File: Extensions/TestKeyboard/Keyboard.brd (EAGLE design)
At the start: 157.5 x 59.7 mm, 69 parts

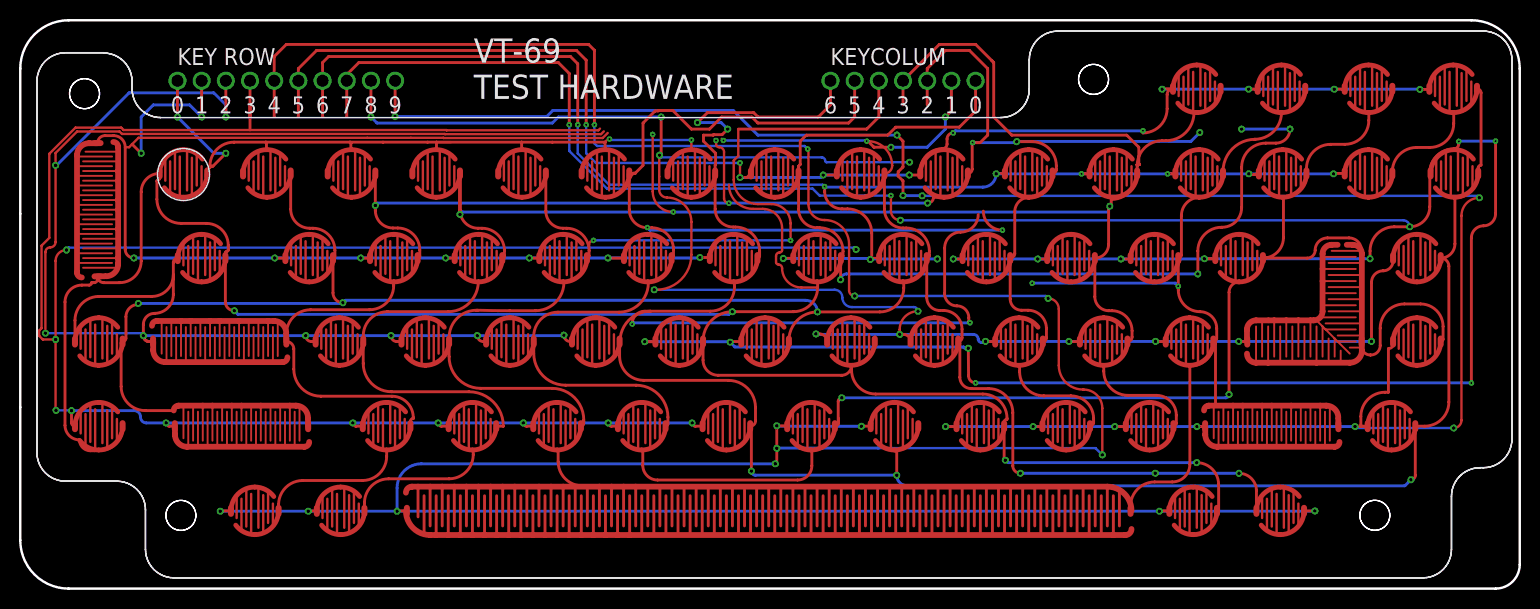
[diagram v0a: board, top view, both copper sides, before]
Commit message: changed MCU test board for FPC cable, other mods, moved test keyboard
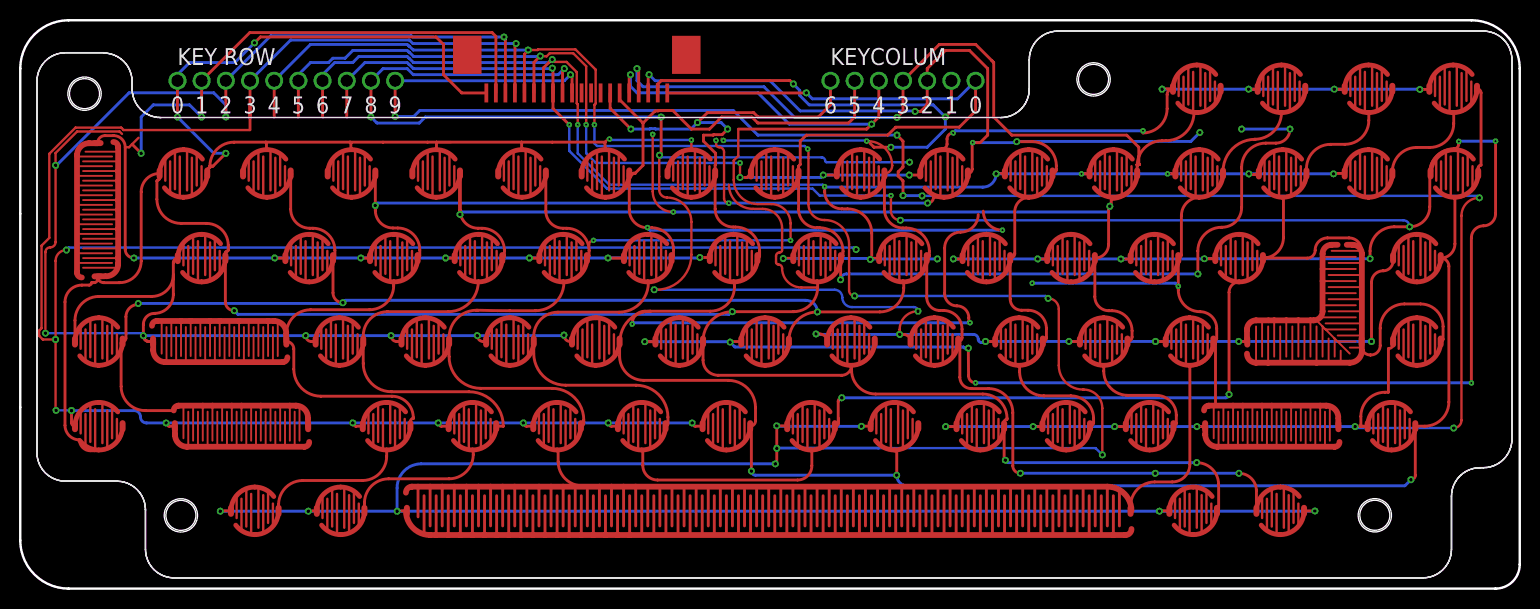
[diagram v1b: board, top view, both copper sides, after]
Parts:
- added U$1: FC1-20-L2-T-WT20PIN, FPC:FC1-20-L2-T-WT
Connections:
- new net KEYCOLUM0: U$1.20
- new net KEYCOLUM1: U$1.19
- new net KEYCOLUM2: U$1.18
- new net KEYCOLUM3: U$1.17
- new net KEYCOLUM4: U$1.16
- new net KEYCOLUM5: U$1.15
- new net KEYCOLUM6: U$1.14
- new net KEYROW0: U$1.1
- new net KEYROW1: U$1.2
- new net KEYROW2: U$1.3
- new net KEYROW3: U$1.4
- new net KEYROW4: U$1.5
- new net KEYROW5: U$1.6
- new net KEYROW6: U$1.7
- new net KEYROW7: U$1.8
- new net KEYROW8: U$1.9
- new net KEYROW9: U$1.10
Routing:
- net KEYROW0: track 100.3 -> 139.4 mm, vias 5 -> 6
- net KEYCOLUM3: track 239.7 -> 274.1 mm, vias 5 -> 7
- net KEYCOLUM0: track 331.6 -> 365.0 mm, vias 9 -> 10
- net KEYCOLUM1: track 241.2 -> 274.3 mm, vias 11 -> 12
- net KEYCOLUM2: track 232.4 -> 265.4 mm, vias 8 -> 10
- net KEYCOLUM4: track 265.3 -> 295.4 mm, vias 5 -> 7
- net KEYROW8: track 190.3 -> 214.3 mm, vias 14 -> 15
- net KEYROW9: track 221.1 -> 241.7 mm, vias 12 -> 13
- net KEYROW2: track 190.7 -> 177.1 mm, vias 9 -> 10
- net KEYCOLUM6: track 270.7 -> 282.7 mm, vias 8 -> 9
- net KEYROW1: track 149.8 -> 139.4 mm
- net KEYCOLUM5: track 279.6 -> 283.8 mm
- net KEYROW5: track 149.6 -> 153.3 mm, vias 12 -> 13
- net KEYROW6: track 159.3 -> 162.2 mm, vias 11 -> 12
- net KEYROW4: track 343.2 -> 345.5 mm, vias 15 -> 16
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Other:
- board text removed: "PENIS"
- board text removed: "VT-69 TEST HARDWARE"
